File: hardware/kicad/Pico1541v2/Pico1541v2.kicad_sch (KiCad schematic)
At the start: 49 parts, among them J1 SWD, J2 Serial, J3 Display/Keys, J4 Micro SD Card, J5 OLED/Key_Hat, J6 OLED, J7 DIN-6, Q1 MMBT3904, SW1 Reset, SW2 Button1, SW3 Button2, SW4 Button3, SW5 Button4, U1 74LS06, U2 SRV05-4

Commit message: More hardware v2 updates
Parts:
- removed R3: 10K, Resistor_SMD:R_0603_1608Metric_Pad0.98x0.95mm_HandSolder, symbol Device:R
- D1: footprint Pico1541 Footprints:LED_D5.0mm-4_RGB_CorrectStaggered_Pins -> Pico1541-footprints:LED_D5.0mm-4_RGB_CorrectStaggered_Pins
- D2: value PWR_STATE -> LED_ACT
- J4: footprint Pico1541 Footprints:MicroSD_HPJF -> Pico1541-footprints:MicroSD_HPJF
- J7: footprint Pico1541 Footprints:DIN-6-240deg -> Pico1541-footprints:DIN-6-240deg
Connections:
- net +3.3V: now also RN1.5 (R4.2), RN1.6 (R3.2), RN1.7 (R2.2), RN1.8 (R1.2); no longer RN1.1 (R1.1), RN1.2 (R2.1), RN1.3 (R3.1), RN1.4 (R4.1)
- net ALED_P: now also RN2.4 (R4.1); no longer RN2.1 (R1.1)
- net SD_CD: now also RN1.4 (R4.1); no longer RN1.5 (R4.2)
- net SD_CLK: now also RN1.2 (R2.1); no longer RN1.7 (R2.2)
- net SD_CMD: now also RN1.3 (R3.1); no longer RN1.6 (R3.2)
- net SD_DAT0: now also RN1.1 (R1.1); no longer RN1.8 (R1.2)
- net SLED_B: now also RN2.1 (R1.1); no longer RN2.4 (R4.1)
- net SLED_G: now also RN2.2 (R2.1); no longer RN2.3 (R3.1)
- net SLED_R: now also RN2.3 (R3.1); no longer RN2.2 (R2.1)
- net at RN2.5 (R4.2): now also D2.1 (KA); no longer D1.4 (BA)
- net at RN2.6 (R3.2): now also D1.2 (RA); no longer D1.3 (GA)
- net at RN2.7 (R2.2): now also D1.3 (GA); no longer D1.2 (RA)
- net at RN2.8 (R1.2): now also D1.4 (BA); no longer D2.1 (KA)
- net SD_DET renamed DET_SD
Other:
- moved on the sheet: RN1, RN2
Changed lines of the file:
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@@
 	)
 	(junction
-		(at 46.99 100.33)
+		(at 127 147.32)
 		(diameter 0)
 		(color 0 0 0 0)
 	)
 	(junction
-		(at 127 147.32)
+		(at 46.99 100.33)
 		(diameter 0)
 		(color 0 0 0 0)
@@
 	)
 	(junction
-		(at 127 144.78)
-		(diameter 0)
-		(color 0 0 0 0)
-	)
-	(junction
 		(at 27.94 190.5)
 		(diameter 0)
@@
 	(wire
 		(pts
-			(xy 127 142.24) (xy 127 144.78)
-		)
-		(stroke
-			(width 0)
-			(type default)
-		)
-	)
-	(wire
-		(pts
 			(xy 50.8 49.53) (xy 50.8 46.99)
 		)
@@
 	(wire
 		(pts
-			(xy 127 144.78) (xy 119.38 144.78)
-		)
-		(stroke
-			(width 0)
-			(type default)
-		)
-	)
-	(wire
-		(pts
 			(xy 209.55 48.26) (xy 219.71 48.26)
 		)
@@
 	(wire
 		(pts
-			(xy 111.76 144.78) (xy 106.68 144.78)
-		)
-		(stroke
-			(width 0)
-			(type default)
-		)
-	)
-	(wire
-		(pts
 			(xy 256.54 128.27) (xy 256.54 133.35)
 		)
@@
 		)
 	)
-	(label "SD_DET"
+	(label "DET_SD"
 		(at 71.12 82.55 180)
 		(effects
@@
 		)
 	)
-	(label "SD_DET"
-		(at 106.68 144.78 180)
-		(effects
-			(font
-				(size 1.27 1.27)
-			)
-			(justify right bottom)
-		)
-	)
 	(label "RESET_RX"
 		(at 123.19 85.09 0)
@@
 		)
 	)
-	(label "SD_DET"
+	(label "DET_SD"
 		(at 77.47 140.97 0)
 		(effects
@@
 	(symbol
 		(lib_id "Device:R_Pack04")
-		(at 115.57 152.4 90)
-		(mirror x)
+		(at 115.57 152.4 270)
 		(unit 1)
 		(body_style 1)
@@
 		(dnp no)
 		(property "Reference" "RN1"
-			(at 110.744 157.226 90)
+			(at 115.824 157.48 90)
 			(show_name no)
 			(do_not_autoplace no)
@@
 		)
 		(property "Value" "10k"
-			(at 110.744 159.766 90)
+			(at 115.824 159.512 90)
 			(show_name no)
 			(do_not_autoplace no)
@@
 	(symbol
 		(lib_id "Device:R_Pack04")
-		(at 146.05 105.41 180)
+		(at 148.59 105.41 0)
+		(mirror x)
 		(unit 1)
 		(body_style 1)
@@
 		(in_pos_files yes)
 		(dnp no)
-		(fields_autoplaced yes)
 		(property "Reference" "RN2"
-			(at 153.67 104.1399 0)
+			(at 140.97 104.1399 0)
 			(show_name no)
 			(do_not_autoplace no)
@@
 		)
 		(property "Value" "330"
-			(at 153.67 106.6799 0)
+			(at 140.97 106.6799 0)
 			(show_name no)
 			(do_not_autoplace no)
@@
 		)
 		(property "Footprint" "Resistor_SMD:R_Array_Convex_4x0603"
-			(at 139.065 105.41 90)
+			(at 155.575 105.41 90)
 			(hide yes)
 			(show_name no)
@@
 		)
 		(property "Datasheet" ""
-			(at 146.05 105.41 0)
+			(at 148.59 105.41 0)
 			(hide yes)
 			(show_name no)
@@
 		)
 		(property "Description" "4 resistor network, parallel topology"
-			(at 146.05 105.41 0)
+			(at 148.59 105.41 0)
 			(hide yes)
 			(show_name no)
@@
 	)
 	(symbol
-		(lib_id "Device:R")
-		(at 115.57 144.78 90)
-		(mirror x)
-		(unit 1)
-		(body_style 1)
-		(exclude_from_sim no)
-		(in_bom yes)
-		(on_board yes)
-		(in_pos_files yes)
-		(dnp no)
-		(property "Reference" "R3"
-			(at 115.57 140.462 90)
-			(show_name no)
-			(do_not_autoplace no)
-			(effects
-				(font
-					(size 1.27 1.27)
-				)
-			)
-		)
-		(property "Value" "10K"
-			(at 115.57 142.494 90)
-			(show_name no)
-			(do_not_autoplace no)
-			(effects
-				(font
-					(size 1.27 1.27)
-				)
-			)
-		)
-		(property "Footprint" "Resistor_SMD:R_0603_1608Metric_Pad0.98x0.95mm_HandSolder"
-			(at 115.57 143.002 90)
-			(hide yes)
-			(show_name no)
-			(do_not_autoplace no)
-			(effects
-				(font
-					(size 1.27 1.27)
-				)
-			)
-		)
-		(property "Datasheet" ""
-			(at 115.57 144.78 0)
-			(hide yes)
-			(show_name no)
-			(do_not_autoplace no)
-			(effects
-				(font
-					(size 1.27 1.27)
-				)
-			)
-		)
-		(property "Description" "Resistor"
-			(at 115.57 144.78 0)
-			(hide yes)
-			(show_name no)
-			(do_not_autoplace no)
-			(effects
-				(font
-					(size 1.27 1.27)
-				)
-			)
-		)
-		(pin "1"
-		)
-		(pin "2"
-		)
-		(instances
-			(project "Pico1541v2"
-				(path "/fb7a9a9a-73a1-4d45-b1f9-1589f10de67b"
-					(reference "R3")
-					(unit 1)
-				)
-			)
-		)
-	)
-	(symbol
 		(lib_id "power:+3.3V")
 		(at 30.48 67.31 270)
@@
 	(symbol
 		(lib_id "power:+3.3V")
-		(at 127 142.24 0)
+		(at 127 144.78 0)
 		(mirror y)
 		(unit 1)
@@
 		(fields_autoplaced yes)
 		(property "Reference" "#PWR015"
-			(at 127 146.05 0)
+			(at 127 148.59 0)
 			(hide yes)
 			(show_name no)
@@
 		)
 		(property "Value" "+3.3V"
-			(at 127 137.16 0)
+			(at 127 139.7 0)
 			(show_name no)
 			(do_not_autoplace no)
@@
 		)
 		(property "Footprint" ""
-			(at 127 142.24 0)
+			(at 127 144.78 0)
 			(hide yes)
 			(show_name no)
@@
 		)
 		(property "Datasheet" ""
-			(at 127 142.24 0)
+			(at 127 144.78 0)
 			(hide yes)
 			(show_name no)
@@
 		)
 		(property "Description" "Power symbol creates a global label with name \"+3.3V\""
-			(at 127 142.24 0)
+			(at 127 144.78 0)
 			(hide yes)
 			(show_name no)
@@
 			)
 		)
-		(property "Footprint" "Pico1541 Footprints:LED_D5.0mm-4_RGB_CorrectStaggered_Pins"
+		(property "Footprint" "Pico1541-footprints:LED_D5.0mm-4_RGB_CorrectStaggered_Pins"
 			(at 147.32 121.92 0)
 			(hide yes)
@@
 			)
 		)
-		(property "Footprint" "Pico1541 Footprints:DIN-6-240deg"
+		(property "Footprint" "Pico1541-footprints:DIN-6-240deg"
 			(at 259.08 38.1 0)
 			(hide yes)
@@
 			)
 		)
-		(property "Footprint" "Pico1541 Footprints:MicroSD_HPJF"
+		(property "Footprint" "Pico1541-footprints:MicroSD_HPJF"
 			(at -1.27 171.45 0)
 			(hide yes)
@@
 		(dnp no)
 		(property "Reference" "D2"
-			(at 159.258 122.428 90)
+			(at 172.212 124.206 90)
 			(show_name no)
 			(do_not_autoplace no)
@@
 			)
 		)
-		(property "Value" "PWR_STATE"
-			(at 153.162 124.968 90)
+		(property "Value" "LED_ACT"
+			(at 169.672 126.492 90)
 			(show_name no)
 			(do_not_autoplace no)
@@
 		(lib_id "Device:C")
 		(at 127 162.56 0)
-		(mirror y)
 		(unit 1)
 		(body_style 1)
@@
 		(dnp no)
 		(property "Reference" "C3"
-			(at 133.35 162.306 0)
+			(at 120.65 162.306 0)
 			(show_name no)
 			(do_not_autoplace no)
@@
 		)
 		(property "Value" "10u"
-			(at 133.35 164.846 0)
+			(at 120.65 164.846 0)
 			(show_name no)
 			(do_not_autoplace no)
@@
 		)
 		(property "Footprint" "Capacitor_SMD:C_0603_1608Metric_Pad1.08x0.95mm_HandSolder"
-			(at 126.0348 166.37 0)
+			(at 127.9652 166.37 0)
 			(hide yes)
 			(show_name no)

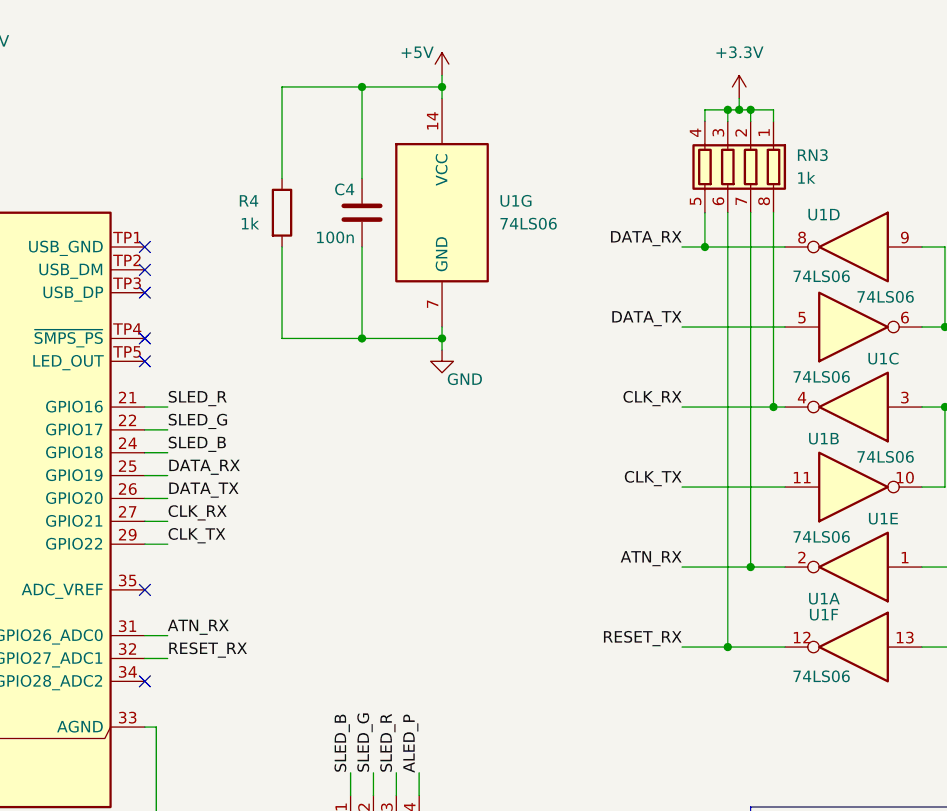
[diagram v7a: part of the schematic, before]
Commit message: Added 1K pull-up on the data output pin, to make it possible to drive high by configuring the pin as an input. This can be done independently of the pin state, resulting in a hardware ATN ack function that is both simple and bullet proof.
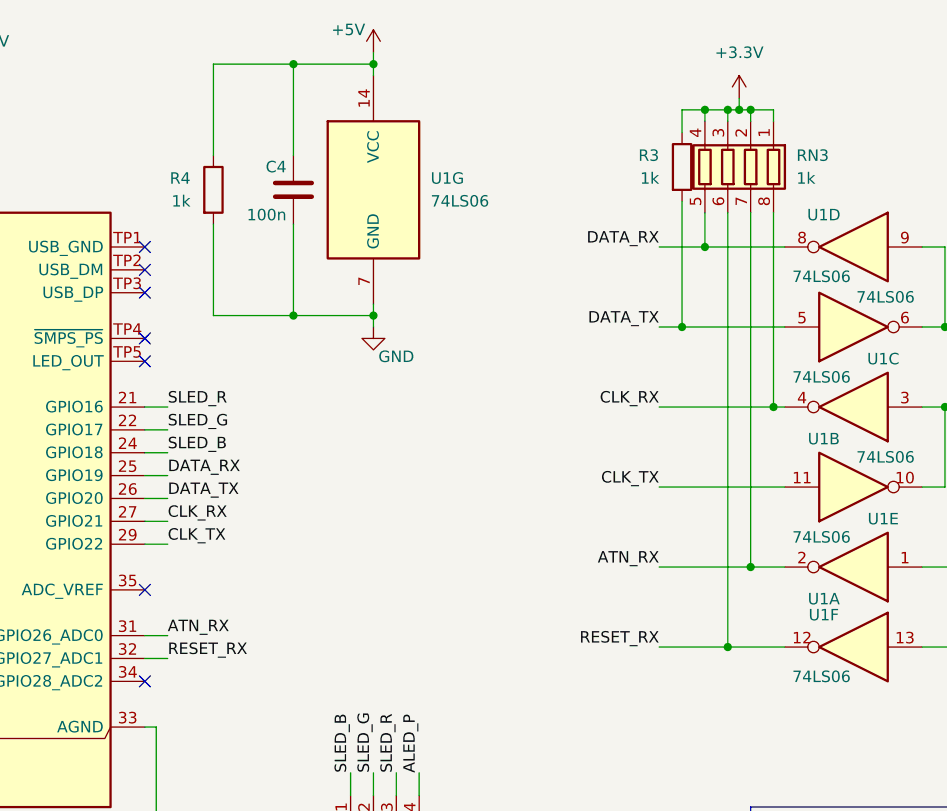
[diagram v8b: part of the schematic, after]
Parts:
- added R3: 1k, Resistor_SMD:R_0603_1608Metric_Pad0.98x0.95mm_HandSolder, symbol Device:R
- D1: footprint Pico1541-footprints:LED_D5.0mm-4_RGB_CorrectStaggered_Pins -> Pico-1541 Footprints:LED_D5.0mm-4_RGB_CorrectStaggered_Pins
- J4: footprint Pico1541-footprints:MicroSD_HPJF -> Pico-1541 Footprints:MicroSD_HPJF
- J7: footprint Pico1541-footprints:DIN-6-240deg -> Pico-1541 Footprints:DIN-6-240deg
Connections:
- net +3.3V: now also R3.1
- net DATA_TX: now also R3.2
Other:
- moved on the sheet: C4, R4, U1G
